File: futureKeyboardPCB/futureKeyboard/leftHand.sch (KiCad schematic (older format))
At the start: 36 parts

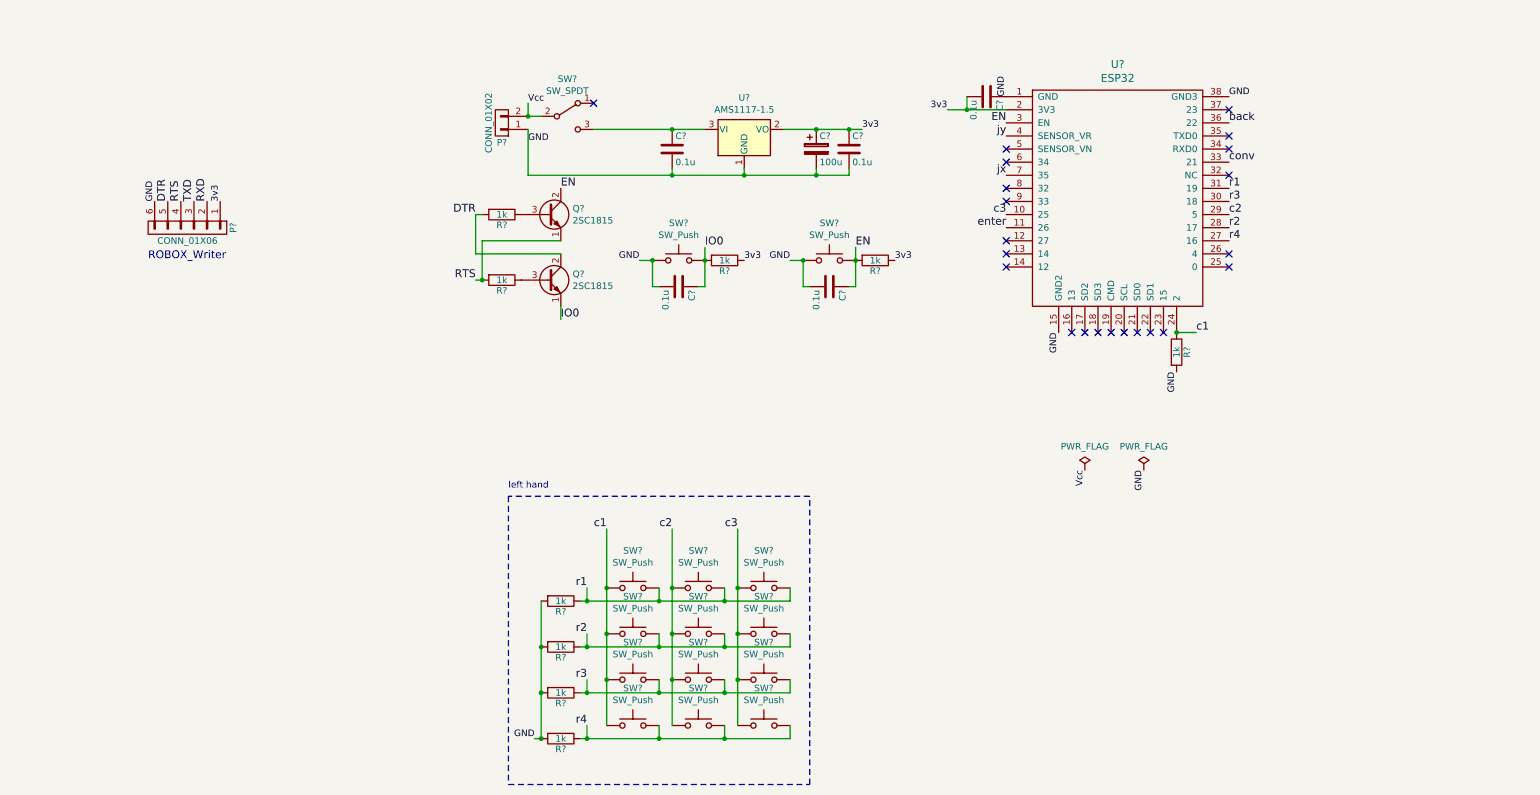
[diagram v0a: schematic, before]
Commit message: add left hand circuit on .sch file
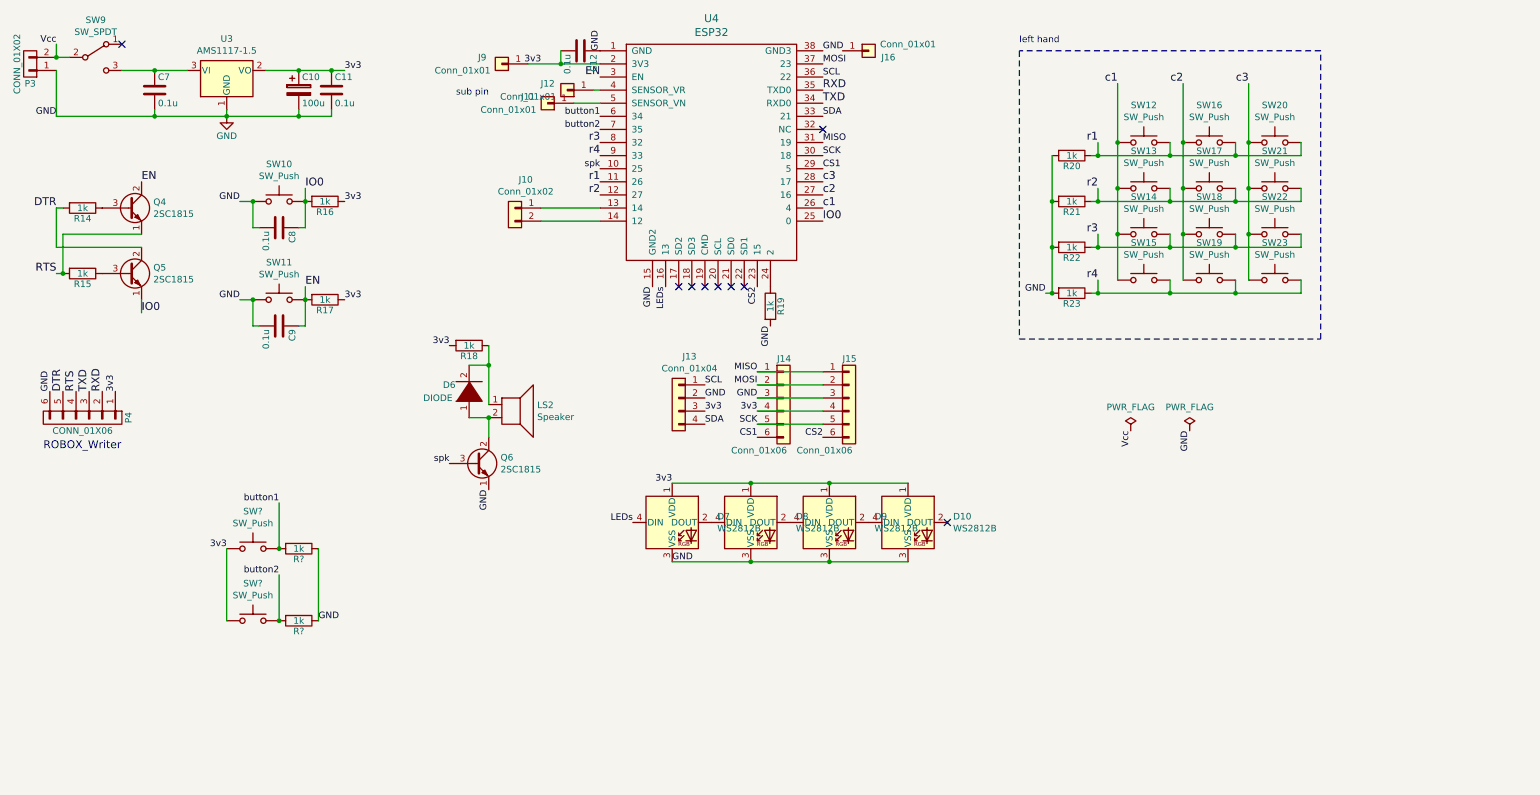
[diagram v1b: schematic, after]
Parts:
- removed C? (x5): 0.1u, akizukit:SMD-2012, symbol Hyper_Board_Traser-rescue:C
- removed C?: 100u, Capacitor_THT:CP_Radial_D4.0mm_P2.00mm, symbol Hyper_Board_Traser-rescue:CP
- removed P?: CONN_01X06, Connector_PinHeader_2.54mm:PinHeader_1x06_P2.54mm_Vertical, symbol Hyper_Board_Traser-rescue:CONN_01X06
- removed P?: CONN_01X02, akizukit:Connector_EH_2pin, symbol Hyper_Board_Traser-rescue:CONN_01X02
- removed Q? (x2): 2SC1815, Package_TO_SOT_THT:TO-92_Inline, symbol Transistor_BJT:2SC1815
- removed R? (x5): 1k, akizukit:SMD-1608, symbol Hyper_Board_Traser-rescue:R
- removed SW?: SW_SPDT, Connector_PinHeader_2.54mm:PinHeader_1x03_P2.54mm_Vertical, symbol Switch:SW_SPDT
- removed SW? (x2): SW_Push, akizukit:SMD_SW, symbol Switch:SW_Push
- removed U?: ESP32, akizukit:ESP-WROOM-32, symbol akizukit:ESP32
- removed U?: AMS1117-1.5, Package_TO_SOT_SMD:SOT-223-3_TabPin2, symbol Regulator_Linear:AMS1117-1.5
- added C10: 100u, Capacitor_THT:CP_Radial_D4.0mm_P2.00mm, symbol Hyper_Board_Traser-rescue:CP
- added C11, C12, C7, C8, C9: 0.1u, akizukit:SMD-2012, symbol Hyper_Board_Traser-rescue:C
- added D10, D7, D8, D9: WS2812B, LED_SMD:LED_WS2812B_PLCC4_5.0x5.0mm_P3.2mm, symbol LED:WS2812B
- added D6: DIODE, symbol pspice:DIODE
- added J10: Conn_01x02, symbol Connector_Generic:Conn_01x02
- added J11, J12, J16, J9: Conn_01x01, symbol Connector_Generic:Conn_01x01
- added J13: Conn_01x04, symbol Connector_Generic:Conn_01x04
- added J14, J15: Conn_01x06, symbol Connector_Generic:Conn_01x06
- added LS2: Speaker, symbol Device:Speaker
- added P3: CONN_01X02, akizukit:Connector_EH_2pin, symbol Hyper_Board_Traser-rescue:CONN_01X02
- added P4: CONN_01X06, Connector_PinHeader_2.54mm:PinHeader_1x06_P2.54mm_Vertical, symbol Hyper_Board_Traser-rescue:CONN_01X06
- added Q4, Q5, Q6: 2SC1815, Package_TO_SOT_THT:TO-92_Inline, symbol Transistor_BJT:2SC1815
- added R14, R15, R16, R17, R18, R19, R? (x2): 1k, akizukit:SMD-1608, symbol Hyper_Board_Traser-rescue:R
- added SW10, SW11, SW? (x2): SW_Push, akizukit:SMD_SW, symbol Switch:SW_Push
- added SW9: SW_SPDT, Connector_PinHeader_2.54mm:PinHeader_1x03_P2.54mm_Vertical, symbol Switch:SW_SPDT
- added U3: AMS1117-1.5, Package_TO_SOT_SMD:SOT-223-3_TabPin2, symbol Regulator_Linear:AMS1117-1.5
- added U4: ESP32, akizukit:ESP-WROOM-32, symbol akizukit:ESP32
- gave numbers to parts that had none: 16
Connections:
- net 3v3: now also C10.1, C11.1, C12.2, D10.1 (VDD), D7.1 (VDD), D8.1 (VDD), D9.1 (VDD), J13.3 (Pin_3), J14.4 (Pin_4), J15.4 (Pin_4), J9.1 (Pin_1), P4.1 (P1), R16.1, R17.1, R18.2, SW?.1, SW?.1, U3.2 (VO), U4.2 (3V3)
- net DTR: now also P4.5 (P5), Q5.2 (C), R14.2
- net EN: now also C9.1, Q4.2 (C), R17.2, SW11.2, U4.3 (EN)
- net GND: now also C10.2, C11.2, C12.1, C7.2, C8.2, C9.2, D10.3 (VSS), D7.3 (VSS), D8.3 (VSS), D9.3 (VSS), J13.2 (Pin_2), J14.3 (Pin_3), J15.3 (Pin_3), P3.1 (P1), P4.6 (P6), Q6.1 (E), R19.2, R?.1, R?.1, SW10.1, SW11.1, U3.1 (GND), U4.1 (GND), U4.15 (GND2), U4.38 (GND3)
- net IO0: now also C8.1, Q5.1 (E), R16.2, SW10.2, U4.25 (0)
- net RTS: now also P4.4 (P4), Q4.1 (E), R15.2
- net RXD: now also P4.2 (P2), U4.35 (TXD0)
- net TXD: now also P4.3 (P3), U4.34 (RXD0)
- net Vcc: now also P3.2 (P2), SW9.2 (B)
- net c1: now also U4.26 (4)
- net c2: now also U4.27 (16)
- net c3: now also U4.28 (17)
- net r1: now also U4.11 (26)
- net r2: now also U4.12 (27)
- net r3: now also U4.8 (32)
- net r4: now also U4.9 (33)
- new net: C7.1, SW9.3 (C), U3.3 (VI)
- new net: Q4.3 (B), R14.1
- new net: Q5.3 (B), R15.1
- new net: R19.1, U4.24 (2)
- new net: J10.1 (Pin_1), U4.13 (14)
- new net: J10.2 (Pin_2), U4.14 (12)
- new net: J12.1 (Pin_1), U4.4 (SENSOR_VR)
- new net: J11.1 (Pin_1), U4.5 (SENSOR_VN)
- new net: D6.2 (A), LS2.1, R18.1
- new net: D6.1 (K), LS2.2, Q6.2 (C)
- new net: D7.2 (DOUT), D8.4 (DIN)
- new net: D8.2 (DOUT), D9.4 (DIN)
- new net: D10.4 (DIN), D9.2 (DOUT)
- new net CS1: J14.6 (Pin_6), U4.29 (5)
- new net CS2: J15.6 (Pin_6), U4.23 (15)
- new net LEDs: D7.4 (DIN), U4.16 (13)
- new net MISO: J14.1 (Pin_1), J15.1 (Pin_1), U4.31 (19)
- new net MOSI: J14.2 (Pin_2), J15.2 (Pin_2), U4.37 (23)
- new net SCK: J14.5 (Pin_5), J15.5 (Pin_5), U4.30 (18)
- new net SCL: J13.1 (Pin_1), U4.36 (22)
- new net SDA: J13.4 (Pin_4), U4.33 (21)
- new net button1: R?.2, SW?.2, U4.6 (34)
- new net button2: R?.2, SW?.2, U4.7 (35)
- new net spk: Q6.3 (B), U4.10 (25)
- no-connect marks 22 -> 9
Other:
- note added: "sub pin"
- moved on the sheet: R20, R21, R22, R23, SW12, SW13, SW14, SW15, SW16, SW17, SW18, SW19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

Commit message: create net list
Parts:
- removed U3: AMS1117-1.5, Package_TO_SOT_SMD:SOT-223-3_TabPin2, symbol Regulator_Linear:AMS1117-1.5
- added U3: AMS1117-1.5, Package_TO_SOT_SMD:SOT-223-3_TabPin2, symbol ume-boshi:AMS1117-1.5
- C11, C12, C7, C8, C9: footprint akizukit:SMD-2012 -> akizukit:SMD-1608
- D6: footprint (none) -> Diode_THT:D_A-405_P7.62mm_Horizontal
- J10: footprint (none) -> Connector_PinHeader_2.54mm:PinHeader_1x02_P2.54mm_Vertical
- J11, J12, J16, J9: footprint (none) -> Connector_PinHeader_2.54mm:PinHeader_1x01_P2.54mm_Vertical
- J13: footprint (none) -> Connector_PinHeader_2.54mm:PinHeader_1x04_P2.54mm_Vertical
- J14, J15: footprint (none) -> Connector_PinHeader_2.54mm:PinHeader_1x06_P2.54mm_Vertical
- LS2: footprint (none) -> akizukit:small_speaker
- SW12, SW13, SW14, SW15, SW16, SW17, SW18, SW19, SW20, SW21, SW22, SW23: footprint akizukit:SMD_SW -> Button_Switch_Keyboard:SW_Cherry_MX_1.00u_PCB
- gave numbers to parts that had none: 4
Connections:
- net 3v3: now also U3.2 (VO)
- net GND: now also J16.1 (Pin_1), U3.1 (GND)
- net Vcc: now also C7.1, SW9.3 (C), U3.3 (VI)

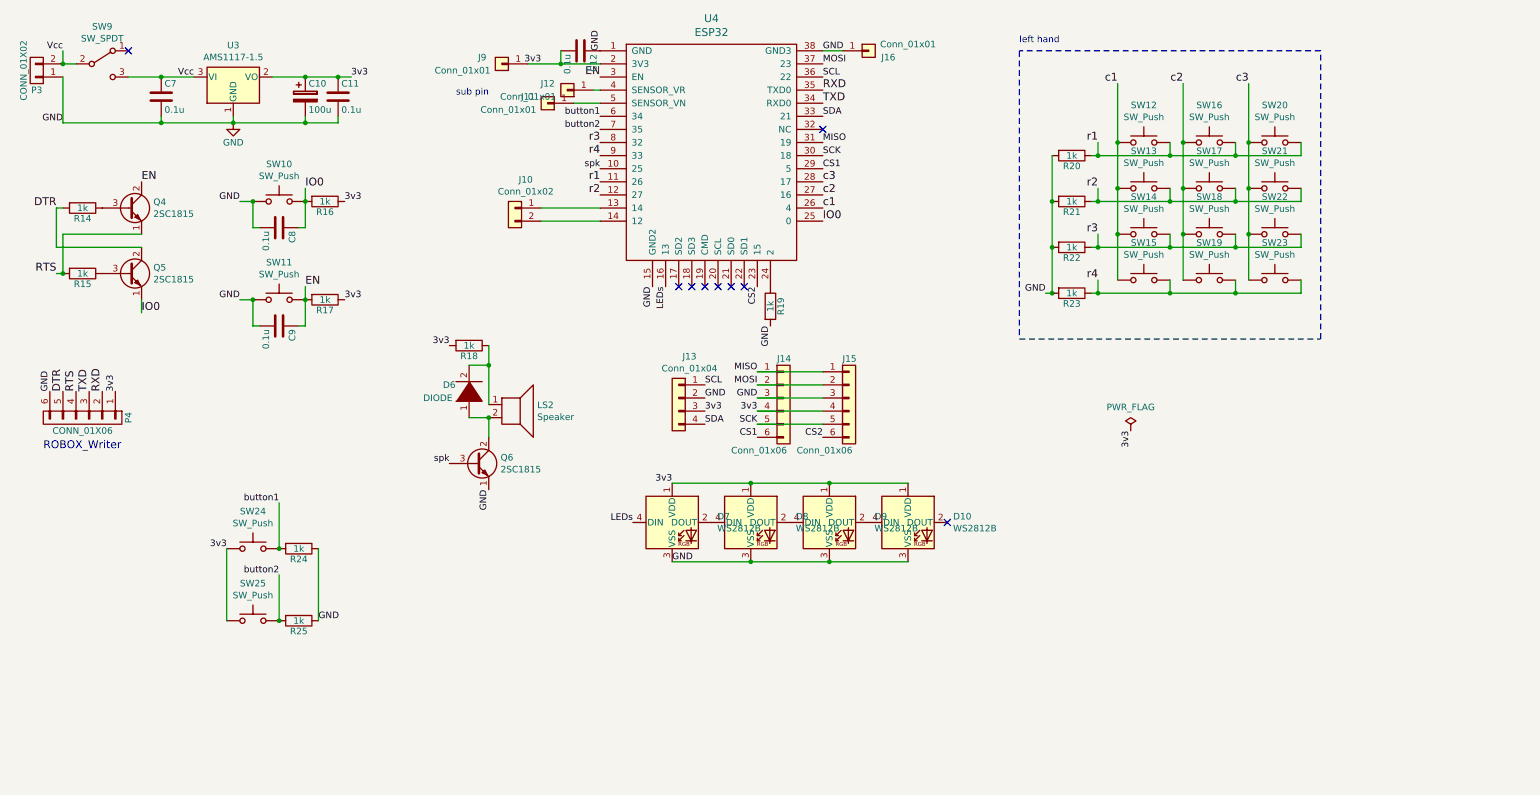
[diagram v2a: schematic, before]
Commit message: fix netlist, and make PCB file
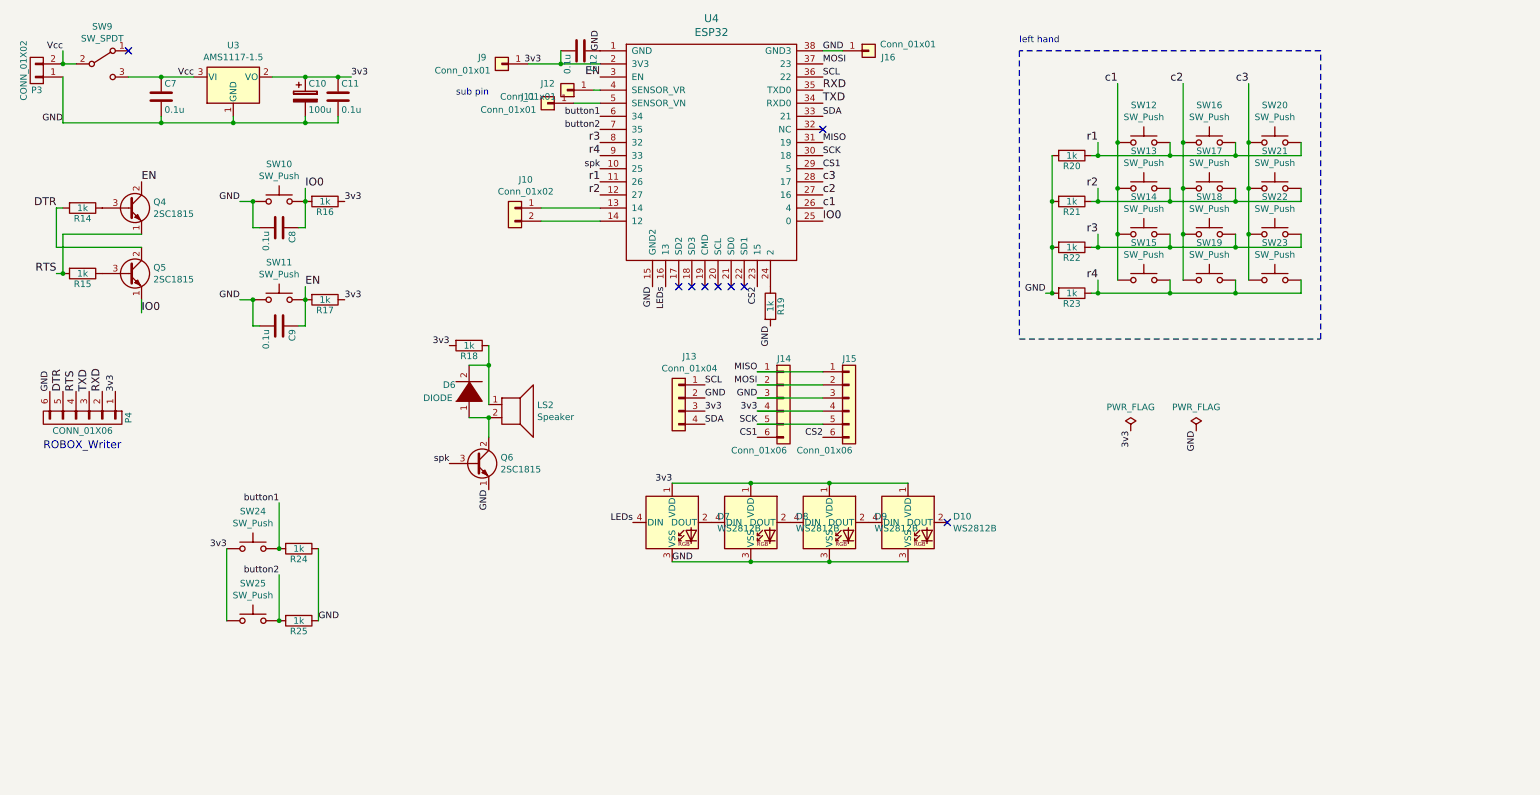
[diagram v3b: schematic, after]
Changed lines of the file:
@@
-	1    0    0    -1
-$EndComp
-$Comp
-L Hyper_Board_Traser-rescue:GND #PWR?
-U 1 1 5F825039
-P 2550 1500
-AR Path="/5F825039" Ref="#PWR?"  Part="1"
-AR Path="/5F548958/5F825039" Ref="#PWR?"  Part="1"
-AR Path="/5F548F89/5F825039" Ref="#PWR01"  Part="1"
-F 0 "#PWR01" H 2550 1250 50  0001 C CNN
-F 1 "GND" H 2550 1350 50  0000 C CNN
-F 2 "" H 2550 1500 50  0000 C CNN
-F 3 "" H 2550 1500 50  0000 C CNN
-	1    2550 1500
 	1    0    0    -1
 $EndComp
@@
 	1    0    0    -1
 $EndComp
+Text Label 9900 3850 3    50   ~ 0
+GND
+$Comp
+L Hyper_Board_Traser-rescue:PWR_FLAG #FLG?
+U 1 1 5F8C9354
+P 9900 3850
+AR Path="/5F8C9354" Ref="#FLG?"  Part="1"
+AR Path="/5F548F89/5F8C9354" Ref="#FLG?"  Part="1"
+F 0 "#FLG?" H 9900 3945 50  0001 C CNN
+F 1 "PWR_FLAG" H 9900 4030 50  0000 C CNN
+F 2 "" H 9900 3850 50  0000 C CNN
+F 3 "" H 9900 3850 50  0000 C CNN
+	1    9900 3850
+	1    0    0    -1
+$EndComp
